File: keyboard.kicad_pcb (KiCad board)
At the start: 2 copper layers, 202.5 x 88.2 mm, 73 parts, among them SW1 SW_SPDT, U1 nice_nano

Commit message: Cut corner version
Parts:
- added H8: Mnt, TestPoint:TestPoint_THTPad_D4.0mm_Drill2.0mm, F.Cu at (54.8, 123.0)
- moved H7 20.8 mm to (31.9, 100.1)
- moved D_18 18.9 mm to (44.6, 99.2)
- moved D_10 18.9 mm to (44.6, 79.0)
- moved D_12 18.9 mm to (44.6, 84.1)
- moved D_14 18.9 mm to (44.6, 89.2)
- moved D_16 18.9 mm to (44.6, 94.2)
- moved D_11 18.9 mm to (44.6, 81.5)
- moved D_13 18.9 mm to (44.6, 86.6)
- moved D_15 18.9 mm to (44.6, 91.7)
- moved D_17 18.9 mm to (44.6, 96.8)
- moved D_24 10.8 mm to (64.5, 104.6)
- moved D_26 10.8 mm to (64.5, 109.7)
- moved D_23 10.8 mm to (64.5, 102.1)
- moved D_25 10.8 mm to (64.5, 107.2)
- moved D_19 7.17 mm to (50.8, 102.1)
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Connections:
- H1 pad 1: Net-(H1-Pad1) -> /GND
- H2 pad 1: Net-(H2-Pad1) -> /BATIN
- SW1 pad 1: Net-(H1-Pad1) -> unconnected-(SW1-Pad1)
- SW1 pad 2: /GND -> /BATIN
- SW1 pad 3: unconnected-(SW1-Pad3) -> /BATIN
- U1 pad 14: unconnected-(U1-Pad14) -> col6
- U1 pad 15: col6 -> col5
- U1 pad 24: Net-(H2-Pad1) -> /BATIN
- U1 pad 7: unconnected-(U1-Pad7) -> col9
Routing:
- net col5: track 52.9 -> 138.5 mm
- net /BATIN: track 0.00 -> 61.7 mm
- net col9: track 5.20 -> 66.1 mm
- net Net-(H2-Pad1): track 57.0 -> 0.00 mm
- net Net-(D_18-Pad2): track 191.1 -> 170.0 mm
- net Net-(D_15-Pad2): track 127.4 -> 106.5 mm
- net Net-(D_16-Pad2): track 148.7 -> 127.7 mm
- net Net-(D_13-Pad2): track 85.0 -> 64.0 mm
- net Net-(D_17-Pad2): track 169.9 -> 148.9 mm
- net Net-(D_14-Pad2): track 106.2 -> 85.2 mm
- net Net-(D_12-Pad2): track 63.8 -> 42.8 mm
- net Net-(D_11-Pad2): track 42.6 -> 22.5 mm
- net Net-(D_10-Pad2): track 26.6 -> 7.85 mm
- net Net-(D_25-Pad2): track 126.3 -> 112.3 mm
- net Net-(D_23-Pad2): track 83.8 -> 69.9 mm
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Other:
- board size 202.5 x 88.2 mm -> 202.5 x 90.2 mm
- board text added: "Bat_GND"
- board text added: "Bat_PWR"
- board text added: "D_"
- board text added: "K_29"
- board text added: "row0"
- board text added: "row1"
- board text added: "row2"
- board text added: "row3"

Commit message: First gerber
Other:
- board text added: "JLCJLCJLCJLC"
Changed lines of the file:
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@@
     (effects (font (size 3 4) (thickness 0.5)))
+  )
+  (gr_text "JLCJLCJLCJLC" (at 75.184 61.468) (layer "F.SilkS")
+    (effects (font (size 0.8 0.8) (thickness 0.15)))
   )
   (gr_text "github.com/tjeffree" (at 49.276 37.846) (layer "F.SilkS")

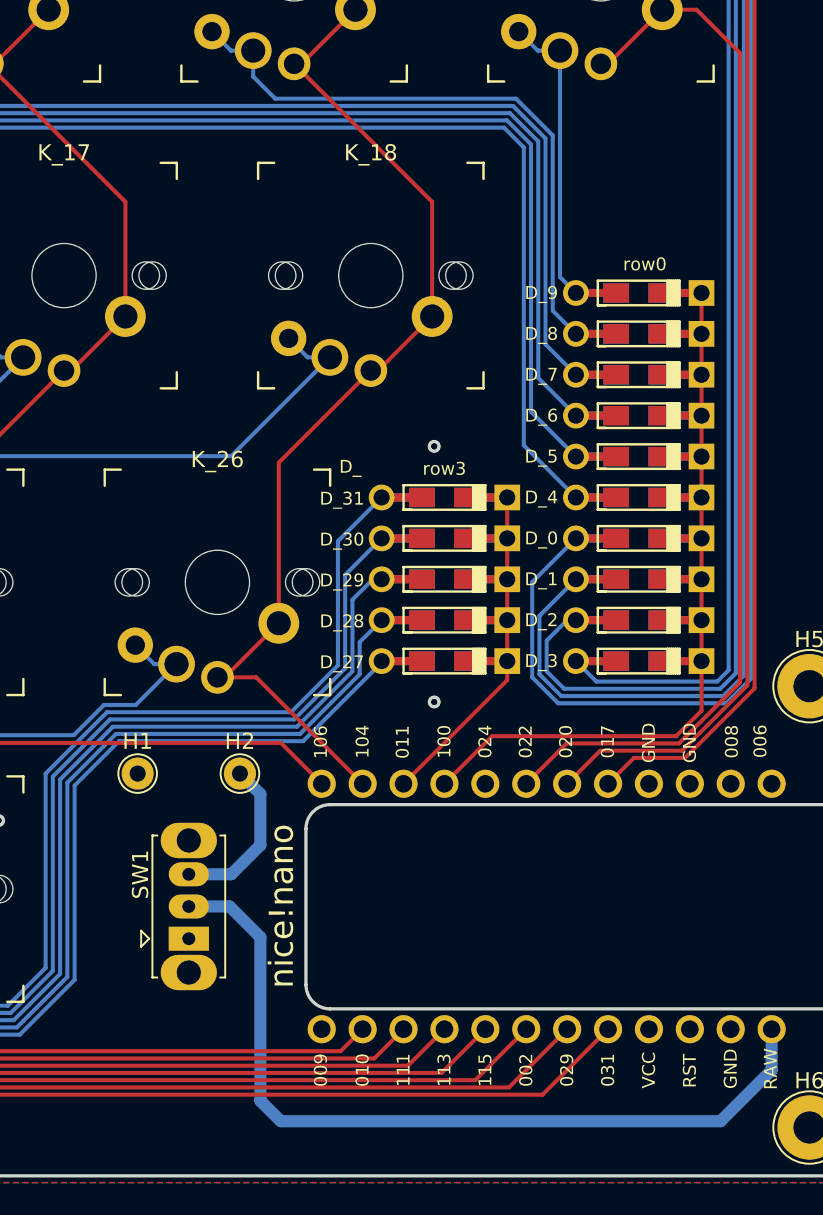
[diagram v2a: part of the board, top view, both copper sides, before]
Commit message: Add reset pins
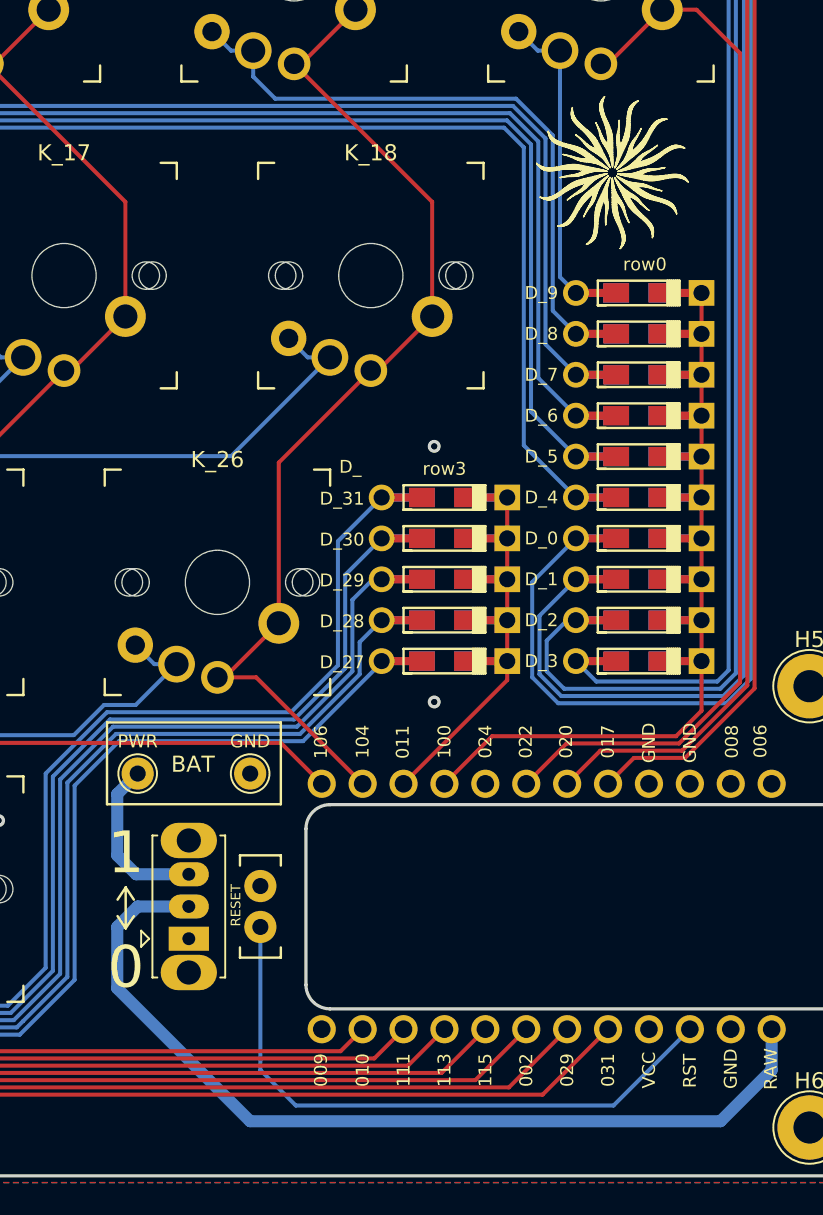
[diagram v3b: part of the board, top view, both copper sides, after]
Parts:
- added TP1: Reset_Pins, ProjectLocal:ResetSW, F.Cu at (194.3, 109.2)
- moved GND 6.99 mm to (193.7, 101.0)
- moved PWR 6.35 mm to (186.7, 101.0)
- renumbered H1 to GND, H2 to PWR
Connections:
- SW1 pad 2: /BATIN -> /BAT
- U1 pad 22: unconnected-(U1-Pad22) -> /RST
- U1 pad 24: /BATIN -> /BAT
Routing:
- net /BAT: track 0.00 -> 56.7 mm
- net /BATIN: track 61.7 -> 10.5 mm
- net /RST: track 0.00 -> 38.4 mm
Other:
- board text added: "0"
- board text added: "1"
- board text added: "BAT"

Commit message: Add prod gerber
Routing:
- net Net-(D_21-Pad2): track 48.8 -> 50.3 mm
- net Net-(D_22-Pad2): track 70.0 -> 71.5 mm
- net Net-(D_20-Pad2): track 28.0 -> 29.5 mm
- net Net-(D_25-Pad2): track 112.3 -> 113.1 mm
- net Net-(D_23-Pad2): track 69.9 -> 70.7 mm
- net Net-(D_26-Pad2): track 133.5 -> 134.3 mm
